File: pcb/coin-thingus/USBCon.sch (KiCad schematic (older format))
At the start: 11 parts, among them J6 Conn_01x05, J7 USB_B_Micro, U6 MCP1703A-3302_SOT23, U7 STM32F042F6Px

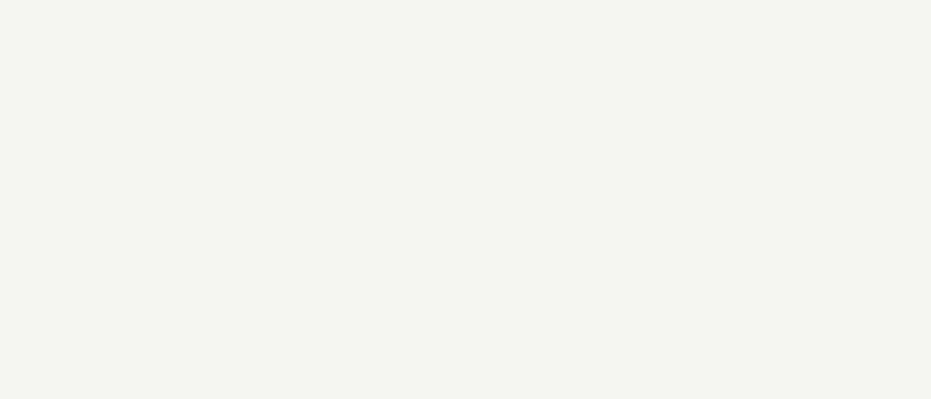
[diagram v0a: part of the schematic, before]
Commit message: Add CERN-OHL-W v2 license
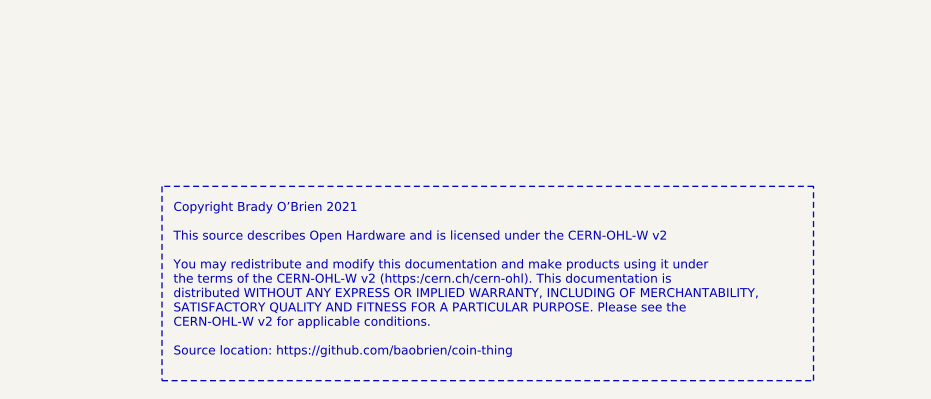
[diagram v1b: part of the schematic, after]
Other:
- note added: "Copyright Brady O’Brien 2021\n\nThis source describes Open Hardware and is licensed under the CERN-OHL-W v2\n\nYou may redistribute and modify this documentation and make products using it under\nthe terms of the CERN-OHL-W v2 (https:/cern.ch/cern-ohl). This documentation is\ndistributed WITHOUT ANY EXPRESS OR IMPLIED WARRANTY, INCLUDING OF MERCHANTABILITY,\nSATISFACTORY QUALITY AND FITNESS FOR A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"
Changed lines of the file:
@@
 Text Label 6550 2800 0    50   ~ 0
 USB_P
+Text Notes 8350 6350 0    39   ~ 0
+Copyright Brady O’Brien 2021\n\nThis source describes Open Hardware and is licensed under the CERN-OHL-W v2\n\nYou may redistribute and modify this documentation and make products using it under\nthe terms of the CERN-OHL-W v2 (https:/cern.ch/cern-ohl). This documentation is\ndistributed WITHOUT ANY EXPRESS OR IMPLIED WARRANTY, INCLUDING OF MERCHANTABILITY,\nSATISFACTORY QUALITY AND FITNESS FOR A PARTICULAR PURPOSE. Please see the\nCERN-OHL-W v2 for applicable conditions.\n\nSource location: https://github.com/baobrien/coin-thing
+Wire Notes Line
+	8300 5600 8300 6450
+Wire Notes Line
+	8300 6450 11150 6450
+Wire Notes Line
+	11150 6450 11150 5600
+Wire Notes Line
+	11150 5600 8300 5600
 $EndSCHEMATC

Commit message: Some work towards v0.2
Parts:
- removed JP1: SolderJumper_2_Open, Jumper:SolderJumper-2_P1.3mm_Open_Pad1.0x1.5mm, symbol Jumper:SolderJumper_2_Open
- added SW1: SW_SPST, Button_Switch_SMD:SW_SPST_TL3342, symbol Switch:SW_SPST
- J7: footprint Connector_USB:USB_Micro-B_Molex-105017-0001 -> coin-trunker:USB_Micro-B_Molex-105017-0001; Part (none) -> U254-051T-4BH23-S2B
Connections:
- net 3V3USB: now also SW1.1 (A)
- net BOOT0: now also SW1.2 (B)
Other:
- note added: "DFU\nBoot"
- note added: "SWD Header"
- moved on the sheet: C10
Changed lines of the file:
@@
 F 0 "J7" H 7620 2789 50  0000 R CNN
 F 1 "USB_B_Micro" H 7620 2698 50  0000 R CNN
-F 2 "Connector_USB:USB_Micro-B_Molex-105017-0001" H 8000 2750 50  0001 C CNN
+F 2 "coin-trunker:USB_Micro-B_Molex-105017-0001" H 8000 2750 50  0001 C CNN
 F 3 "~" H 8000 2750 50  0001 C CNN
+F 4 "U254-051T-4BH23-S2B" H 7850 2800 50  0001 C CNN "Part"
 	1    7850 2800
 	-1   0    0    -1
@@
 L Device:C C10
 U 1 1 5FAEC7BC
-P 2800 2750
-F 0 "C10" H 2915 2796 50  0000 L CNN
-F 1 ".1uF" H 2915 2705 50  0000 L CNN
-F 2 "Capacitor_SMD:C_0603_1608Metric" H 2838 2600 50  0001 C CNN
-F 3 "~" H 2800 2750 50  0001 C CNN
-	1    2800 2750
+P 1650 3100
+F 0 "C10" H 1765 3146 50  0000 L CNN
+F 1 ".1uF" H 1765 3055 50  0000 L CNN
+F 2 "Capacitor_SMD:C_0603_1608Metric" H 1688 2950 50  0001 C CNN
+F 3 "~" H 1650 3100 50  0001 C CNN
+	1    1650 3100
 	1    0    0    -1
 $EndComp
@@
 L power:GND #PWR0123
 U 1 1 5FAED96D
-P 2800 3000
-F 0 "#PWR0123" H 2800 2750 50  0001 C CNN
-F 1 "GND" H 2805 2827 50  0000 C CNN
-F 2 "" H 2800 3000 50  0001 C CNN
-F 3 "" H 2800 3000 50  0001 C CNN
-	1    2800 3000
-	1    0    0    -1
-$EndComp
-Wire Wire Line
-	2800 3000 2800 2900
+P 1650 3350
+F 0 "#PWR0123" H 1650 3100 50  0001 C CNN
+F 1 "GND" H 1655 3177 50  0000 C CNN
+F 2 "" H 1650 3350 50  0001 C CNN
+F 3 "" H 1650 3350 50  0001 C CNN
+	1    1650 3350
+	1    0    0    -1
+$EndComp
+Wire Wire Line
+	1650 3350 1650 3250
 $Comp
 L power:GND #PWR0124
@@
 	7300 3250 7300 3400
 Wire Wire Line
-	2800 2600 2800 2450
-Wire Wire Line
-	2800 2450 3050 2450
-Text Label 3050 2450 2    50   ~ 0
+	1650 2950 1650 2800
+Wire Wire Line
+	1650 2800 1900 2800
+Text Label 1900 2800 2    50   ~ 0
 3V3M
 $Comp
@@
 NoConn ~ 5250 2800
 NoConn ~ 5250 2900
-$Comp
-L Jumper:SolderJumper_2_Open JP1
-U 1 1 5FD8F9A6
-P 3350 3150
-F 0 "JP1" V 3304 3218 50  0000 L CNN
-F 1 "SolderJumper_2_Open" V 3395 3218 50  0000 L CNN
-F 2 "Jumper:SolderJumper-2_P1.3mm_Open_Pad1.0x1.5mm" H 3350 3150 50  0001 C CNN
-F 3 "~" H 3350 3150 50  0001 C CNN
-	1    3350 3150
-	0    1    1    0
-$EndComp
-Wire Wire Line
-	3500 3400 3350 3400
-Wire Wire Line
-	3350 3400 3350 3300
 Connection ~ 3500 3400
-Wire Wire Line
-	3350 3000 3350 2750
-Text Label 3550 2750 2    50   ~ 0
-3V3M
-Wire Wire Line
-	3550 2750 3350 2750
 Text Label 6550 2900 0    50   ~ 0
 USB_N
@@
 Wire Notes Line
 	11150 5600 8300 5600
+$Comp
+L Switch:SW_SPST SW1
+U 1 1 6034D695
+P 3000 3400
+F 0 "SW1" H 3000 3635 50  0000 C CNN
+F 1 "SW_SPST" H 3000 3544 50  0000 C CNN
+F 2 "Button_Switch_SMD:SW_SPST_TL3342" H 3000 3400 50  0001 C CNN
+F 3 "~" H 3000 3400 50  0001 C CNN
+F 4 "TS-1187A-C-G-B" H 3000 3400 50  0001 C CNN "Part"
+	1    3000 3400
+	1    0    0    -1
+$EndComp
+Text Label 2450 3400 0    50   ~ 0
+3V3M
+Wire Wire Line
+	2450 3400 2800 3400
+Wire Wire Line
+	3200 3400 3500 3400
+Text Notes 2900 3600 0    50   ~ 0
+DFU\nBoot
+Text Notes 3550 1200 0    50   ~ 0
+SWD Header
 $EndSCHEMATC

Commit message: HV test board; A bunch of work towards v0.2
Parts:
- added D13: D_TVS_x2_AAC, Package_TO_SOT_SMD:SOT-23, symbol Device:D_TVS_x2_AAC
- added D14: LED, LED_SMD:LED_0603_1608Metric, symbol Device:LED
- added Q2, Q3: BSS123L, Package_TO_SOT_SMD:SOT-23, symbol Transistor_FET:BSS138
- added R26: 470, Resistor_SMD:R_0603_1608Metric, symbol Device:R_US
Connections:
- net 3V3USB: now also Q2.1 (G), Q3.1 (G)
- net GND: now also D13.3 (common), D14.1 (K)
- net SCL: now also Q3.3 (D); no longer U7.3 (PF1)
- net SDA: now also Q2.3 (D); no longer U7.2 (PF0)
- net USB_N: now also D13.1 (A1)
- net USB_P: now also D13.2 (A2)
- net at U7.6 (PA0): now also R26.2
- new net: Q2.2 (S), U7.2 (PF0)
- new net: Q3.2 (S), U7.3 (PF1)
- new net: D14.2 (A), R26.1
- no-connect marks 9 -> 8
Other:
- note added: "I2C 'Level Converters' \nto isolate MCU from RPI\n"
- moved on the sheet: C10
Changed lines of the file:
@@
 $EndComp
-Wire Wire Line
-	5250 3100 6500 3100
 Wire Wire Line
 	6500 3100 6500 2900
@@
 L Device:C C10
 U 1 1 5FAEC7BC
-P 1650 3100
-F 0 "C10" H 1765 3146 50  0000 L CNN
-F 1 ".1uF" H 1765 3055 50  0000 L CNN
-F 2 "Capacitor_SMD:C_0603_1608Metric" H 1688 2950 50  0001 C CNN
-F 3 "~" H 1650 3100 50  0001 C CNN
-	1    1650 3100
+P 5300 4300
+F 0 "C10" H 5415 4346 50  0000 L CNN
+F 1 ".1uF" H 5415 4255 50  0000 L CNN
+F 2 "Capacitor_SMD:C_0603_1608Metric" H 5338 4150 50  0001 C CNN
+F 3 "~" H 5300 4300 50  0001 C CNN
+	1    5300 4300
 	1    0    0    -1
 $EndComp
@@
 L power:GND #PWR0123
 U 1 1 5FAED96D
-P 1650 3350
-F 0 "#PWR0123" H 1650 3100 50  0001 C CNN
-F 1 "GND" H 1655 3177 50  0000 C CNN
-F 2 "" H 1650 3350 50  0001 C CNN
-F 3 "" H 1650 3350 50  0001 C CNN
-	1    1650 3350
-	1    0    0    -1
-$EndComp
-Wire Wire Line
-	1650 3350 1650 3250
+P 5300 4550
+F 0 "#PWR0123" H 5300 4300 50  0001 C CNN
+F 1 "GND" H 5305 4377 50  0000 C CNN
+F 2 "" H 5300 4550 50  0001 C CNN
+F 3 "" H 5300 4550 50  0001 C CNN
+	1    5300 4550
+	1    0    0    -1
+$EndComp
+Wire Wire Line
+	5300 4550 5300 4450
 $Comp
 L power:GND #PWR0124
@@
 	7300 3250 7300 3400
 Wire Wire Line
-	1650 2950 1650 2800
-Wire Wire Line
-	1650 2800 1900 2800
-Text Label 1900 2800 2    50   ~ 0
+	5300 4150 5300 4000
+Wire Wire Line
+	5300 4000 5550 4000
+Text Label 5550 4000 2    50   ~ 0
 3V3M
 $Comp
@@
 NoConn ~ 5250 3000
 NoConn ~ 4050 3300
-Text HLabel 3850 3000 0    50   BiDi ~ 0
+Text HLabel 1150 2500 0    50   BiDi ~ 0
 SDA
-Wire Wire Line
-	3850 3000 4050 3000
-Text HLabel 3850 3100 0    50   BiDi ~ 0
+Text HLabel 1150 3100 0    50   BiDi ~ 0
 SCL
-Wire Wire Line
-	3850 3100 4050 3100
-NoConn ~ 5250 2300
 NoConn ~ 5250 2400
 NoConn ~ 5250 2500
@@
 Text Notes 3550 1200 0    50   ~ 0
 SWD Header
+$Comp
+L Transistor_FET:BSS138 Q?
+U 1 1 60427585
+P 1750 2400
+AR Path="/60427585" Ref="Q?"  Part="1"
+AR Path="/5FDC9904/60427585" Ref="Q2"  Part="1"
+F 0 "Q2" V 1750 2150 50  0000 L CNN
+F 1 "BSS123L" V 1650 1950 50  0000 L CNN
+F 2 "Package_TO_SOT_SMD:SOT-23" H 1950 2325 50  0001 L CIN
+F 3 "https://www.fairchildsemi.com/datasheets/BS/BSS138.pdf" H 1750 2400 50  0001 L CNN
+	1    1750 2400
+	0    -1   1    0
+$EndComp
+Wire Wire Line
+	2400 3000 2400 2500
+Wire Wire Line
+	2400 2500 1950 2500
+Wire Wire Line
+	2400 3000 4050 3000
+Wire Wire Line
+	1150 2500 1550 2500
+Text Label 2100 2050 2    50   ~ 0
+3V3M
+Wire Wire Line
+	2100 2050 1750 2050
+Wire Wire Line
+	1750 2050 1750 2200
+$Comp
+L Transistor_FET:BSS138 Q?
+U 1 1 60436D03
+P 1750 3000
+AR Path="/60436D03" Ref="Q?"  Part="1"
+AR Path="/5FDC9904/60436D03" Ref="Q3"  Part="1"
+F 0 "Q3" V 1750 2750 50  0000 L CNN
+F 1 "BSS123L" V 1650 2550 50  0000 L CNN
+F 2 "Package_TO_SOT_SMD:SOT-23" H 1950 2925 50  0001 L CIN
+F 3 "https://www.fairchildsemi.com/datasheets/BS/BSS138.pdf" H 1750 3000 50  0001 L CNN
+	1    1750 3000
+	0    -1   1    0
+$EndComp
+Text Notes 1200 3500 0    50   ~ 0
+I2C 'Level Converters' \nto isolate MCU from RPI\n
+Wire Wire Line
+	1950 3100 4050 3100
+Wire Wire Line
+	1150 3100 1550 3100
+Wire Wire Line
+	1750 2800 1750 2700
+Wire Wire Line
+	1750 2700 1450 2700
+Wire Wire Line
+	1450 2700 1450 2050
+Wire Wire Line
+	1450 2050 1750 2050
+Connection ~ 1750 2050
+$Comp
+L Device:D_TVS_x2_AAC D13
+U 1 1 6051E49B
+P 6000 2350
+F 0 "D13" H 6000 2567 50  0000 C CNN
+F 1 "D_TVS_x2_AAC" H 6000 2476 50  0000 C CNN
+F 2 "Package_TO_SOT_SMD:SOT-23" H 5850 2350 50  0001 C CNN
+F 3 "~" H 5850 2350 50  0001 C CNN
+	1    6000 2350
+	1    0    0    -1
+$EndComp
+$Comp
+L power:GND #PWR0130
+U 1 1 60520E3D
+P 6000 2750
+F 0 "#PWR0130" H 6000 2500 50  0001 C CNN
+F 1 "GND" H 6005 2577 50  0000 C CNN
+F 2 "" H 6000 2750 50  0001 C CNN
+F 3 "" H 6000 2750 50  0001 C CNN
+	1    6000 2750
+	1    0    0    -1
+$EndComp
+Wire Wire Line
+	5250 3100 5600 3100
+Wire Wire Line
+	6350 2350 6400 2350
+Wire Wire Line
+	6400 2350 6400 2800
+Connection ~ 6400 2800
+Wire Wire Line
+	5650 2350 5600 2350
+Wire Wire Line
+	5600 2350 5600 3100
+Connection ~ 5600 3100
+Wire Wire Line
+	5600 3100 6500 3100
+Wire Wire Line
+	6000 2500 6000 2750
+$Comp
+L Device:LED D?
+U 1 1 6052FA5C
+P 6150 1600
+AR Path="/6052FA5C" Ref="D?"  Part="1"
+AR Path="/5FDC9904/6052FA5C" Ref="D14"  Part="1"
+F 0 "D14" H 6150 1450 50  0000 C CNN
+F 1 "LED" H 6000 1450 50  0000 C CNN
+F 2 "LED_SMD:LED_0603_1608Metric" H 6150 1600 50  0001 C CNN
+F 3 "~" H 6150 1600 50  0001 C CNN
+	1    6150 1600
+	-1   0    0    1
+$EndComp
+$Comp
+L Device:R_US R?
+U 1 1 6052FA62
+P 5750 1600
+AR Path="/6052FA62" Ref="R?"  Part="1"
+AR Path="/5FDC9904/6052FA62" Ref="R26"  Part="1"
+F 0 "R26" V 5650 1550 50  0000 R CNN
+F 1 "470" V 5650 1750 50  0000 R CNN
+F 2 "Resistor_SMD:R_0603_1608Metric" V 5790 1590 50  0001 C CNN
+F 3 "~" H 5750 1600 50  0001 C CNN
+	1    5750 1600
+	0    1    1    0
+$EndComp
+Wire Wire Line
+	5900 1600 6000 1600
+Wire Wire Line
+	5250 2300 5450 2300
+Wire Wire Line
+	5450 2300 5450 1600
+Wire Wire Line
+	5450 1600 5600 1600
+Wire Wire Line
+	6300 1600 6450 1600
+Wire Wire Line
+	6450 1600 6450 1800
+$Comp
+L power:GND #PWR0131
+U 1 1 60534C96
+P 6450 1800
+F 0 "#PWR0131" H 6450 1550 50  0001 C CNN
+F 1 "GND" H 6455 1627 50  0000 C CNN
+F 2 "" H 6450 1800 50  0001 C CNN
+F 3 "" H 6450 1800 50  0001 C CNN
+	1    6450 1800
+	1    0    0    -1
+$EndComp
 $EndSCHEMATC

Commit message: Bunch'o work towards v0.2
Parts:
- added R29, R30: 10k, Resistor_SMD:R_0603_1608Metric, symbol Device:R_US
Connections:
- net 3V3USB: now also R29.1, R30.1
- net at Q2.2 (S), U7.2 (PF0): now also R29.2
- net at Q3.2 (S), U7.3 (PF1): now also R30.2
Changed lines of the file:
@@
 	2400 2500 1950 2500
 Wire Wire Line
-	2400 3000 4050 3000
+	2400 3000 2750 3000
 Wire Wire Line
 	1150 2500 1550 2500
@@
 I2C 'Level Converters' \nto isolate MCU from RPI\n
 Wire Wire Line
-	1950 3100 4050 3100
+	1950 3100 3100 3100
 Wire Wire Line
 	1150 3100 1550 3100
@@
 	1    0    0    -1
 $EndComp
+$Comp
+L Device:R_US R29
+U 1 1 60525D10
+P 2750 2650
+F 0 "R29" H 2818 2696 50  0000 L CNN
+F 1 "10k" H 2818 2605 50  0000 L CNN
+F 2 "Resistor_SMD:R_0603_1608Metric" V 2790 2640 50  0001 C CNN
+F 3 "~" H 2750 2650 50  0001 C CNN
+	1    2750 2650
+	1    0    0    -1
+$EndComp
+$Comp
+L Device:R_US R30
+U 1 1 605261A3
+P 3100 2650
+F 0 "R30" H 3168 2696 50  0000 L CNN
+F 1 "10k" H 3168 2605 50  0000 L CNN
+F 2 "Resistor_SMD:R_0603_1608Metric" V 3140 2640 50  0001 C CNN
+F 3 "~" H 3100 2650 50  0001 C CNN
+	1    3100 2650
+	1    0    0    -1
+$EndComp
+Wire Wire Line
+	2750 2800 2750 3000
+Connection ~ 2750 3000
+Wire Wire Line
+	2750 3000 4050 3000
+Wire Wire Line
+	3100 2800 3100 3100
+Connection ~ 3100 3100
+Wire Wire Line
+	3100 3100 4050 3100
+Text Label 3000 2400 2    50   ~ 0
+3V3M
+Wire Wire Line
+	2750 2400 3100 2400
+Wire Wire Line
+	3100 2400 3100 2500
+Wire Wire Line
+	2750 2400 2750 2500
 $EndSCHEMATC

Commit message: V0.2 as ordered
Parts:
- SW1: value SW_SPST -> TS-1187A-C-E-B; Part TS-1187A-C-G-B -> TS-1187A-C-E-B
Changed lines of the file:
@@
 P 3000 3400
 F 0 "SW1" H 3000 3635 50  0000 C CNN
-F 1 "SW_SPST" H 3000 3544 50  0000 C CNN
+F 1 "TS-1187A-C-E-B" H 3000 3544 50  0001 C CNN
 F 2 "Button_Switch_SMD:SW_SPST_TL3342" H 3000 3400 50  0001 C CNN
 F 3 "~" H 3000 3400 50  0001 C CNN
-F 4 "TS-1187A-C-G-B" H 3000 3400 50  0001 C CNN "Part"
+F 4 "TS-1187A-C-E-B" H 3000 3400 50  0001 C CNN "Part"
 	1    3000 3400
 	1    0    0    -1

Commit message: Start work on alternate micro
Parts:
- removed U7: STM32F042F6Px, Package_SO:TSSOP-20_4.4x6.5mm_P0.65mm, symbol coin-trunker-rescue:STM32F042F6Px-MCU_ST_STM32F0
- added U9: STM32F042K6Tx, Package_QFP:LQFP-32_7x7mm_P0.8mm, symbol MCU_ST_STM32F0:STM32F042K6Tx
- R17, R18, R26, R29, R30: footprint Resistor_SMD:R_0603_1608Metric -> Resistor_SMD:R_0402_1005Metric
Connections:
- net 3V3USB: now also U9.1 (VDD), U9.17 (VDDIO2), U9.5 (VDDA)
- net BOOT0: now also U9.31 (PB8)
- net GND: now also U9.16 (VSS), U9.32 (VSSA)
- net NRST: now also U9.4 (NRST)
- net SWCLK: now also U9.24 (PA14)
- net SWDIO: now also U9.25 (PA15)
- net USB_N: now also U9.22 (PA12)
- net USB_P: now also U9.23 (PA13)
- net at Q2.2 (S), R29.2: now also U9.2 (PF0)
- net at Q3.2 (S), R30.2: now also U9.3 (PF1)
- net at R26.2: now also U9.6 (PA0)
- no-connect marks 8 -> 18
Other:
- moved on the sheet: C10, C11, D13, D14, J7, Q2, Q3, R18, R26, R29, R30, SW1
